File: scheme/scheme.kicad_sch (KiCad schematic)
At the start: 3 parts, among them U1 ESP32-WROOM-32, U2 PCM1808

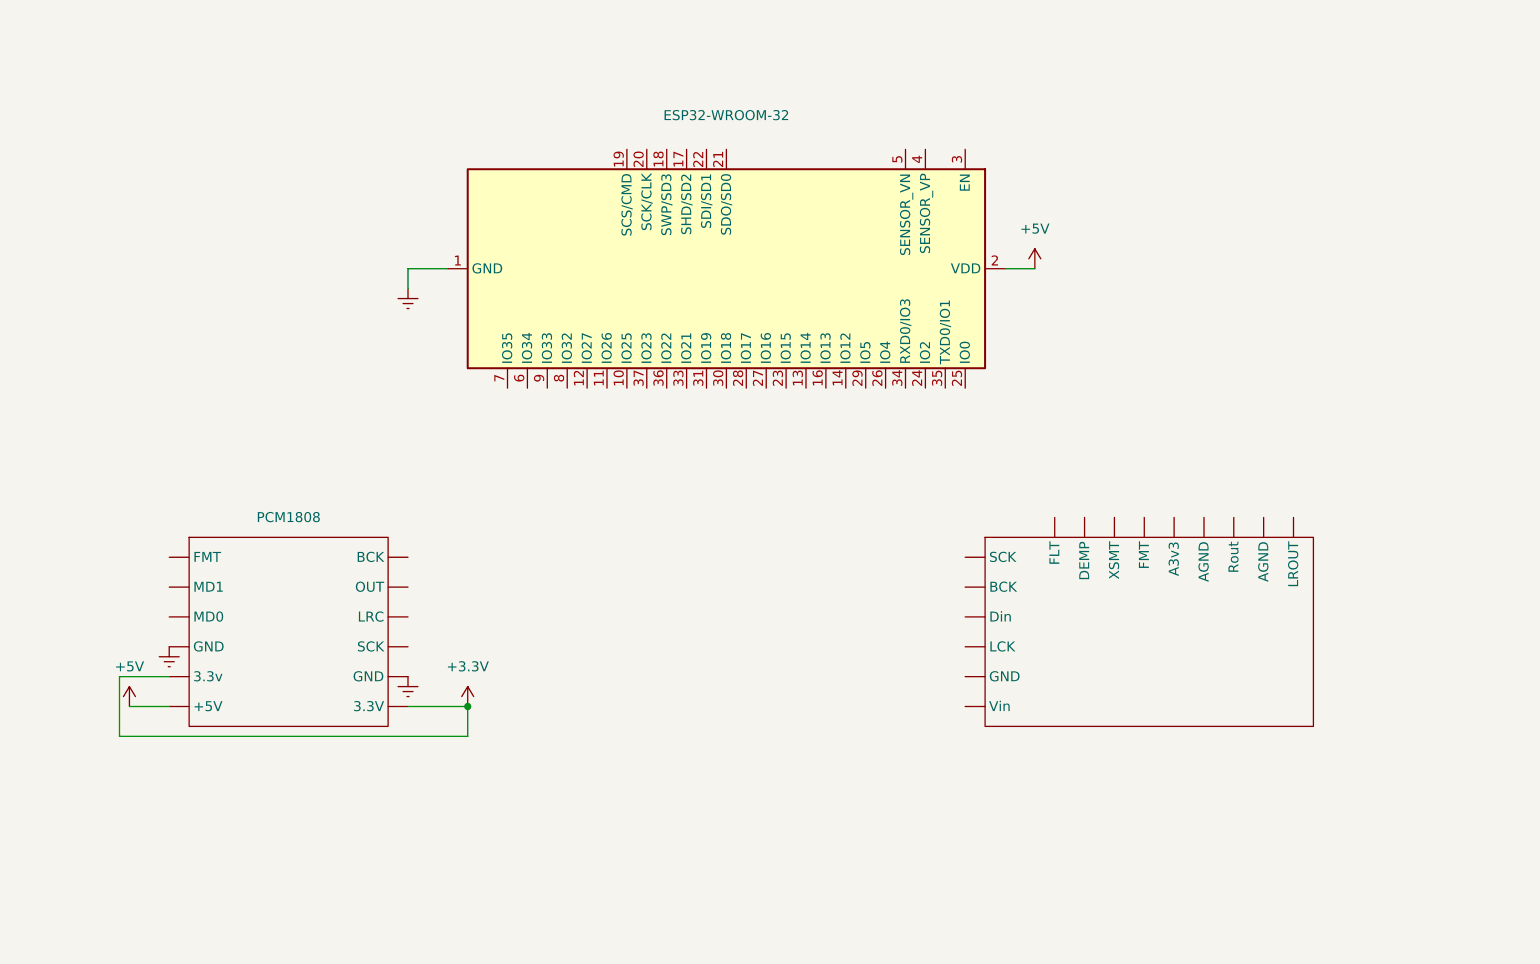
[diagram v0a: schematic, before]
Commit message: Add project scheme and update README
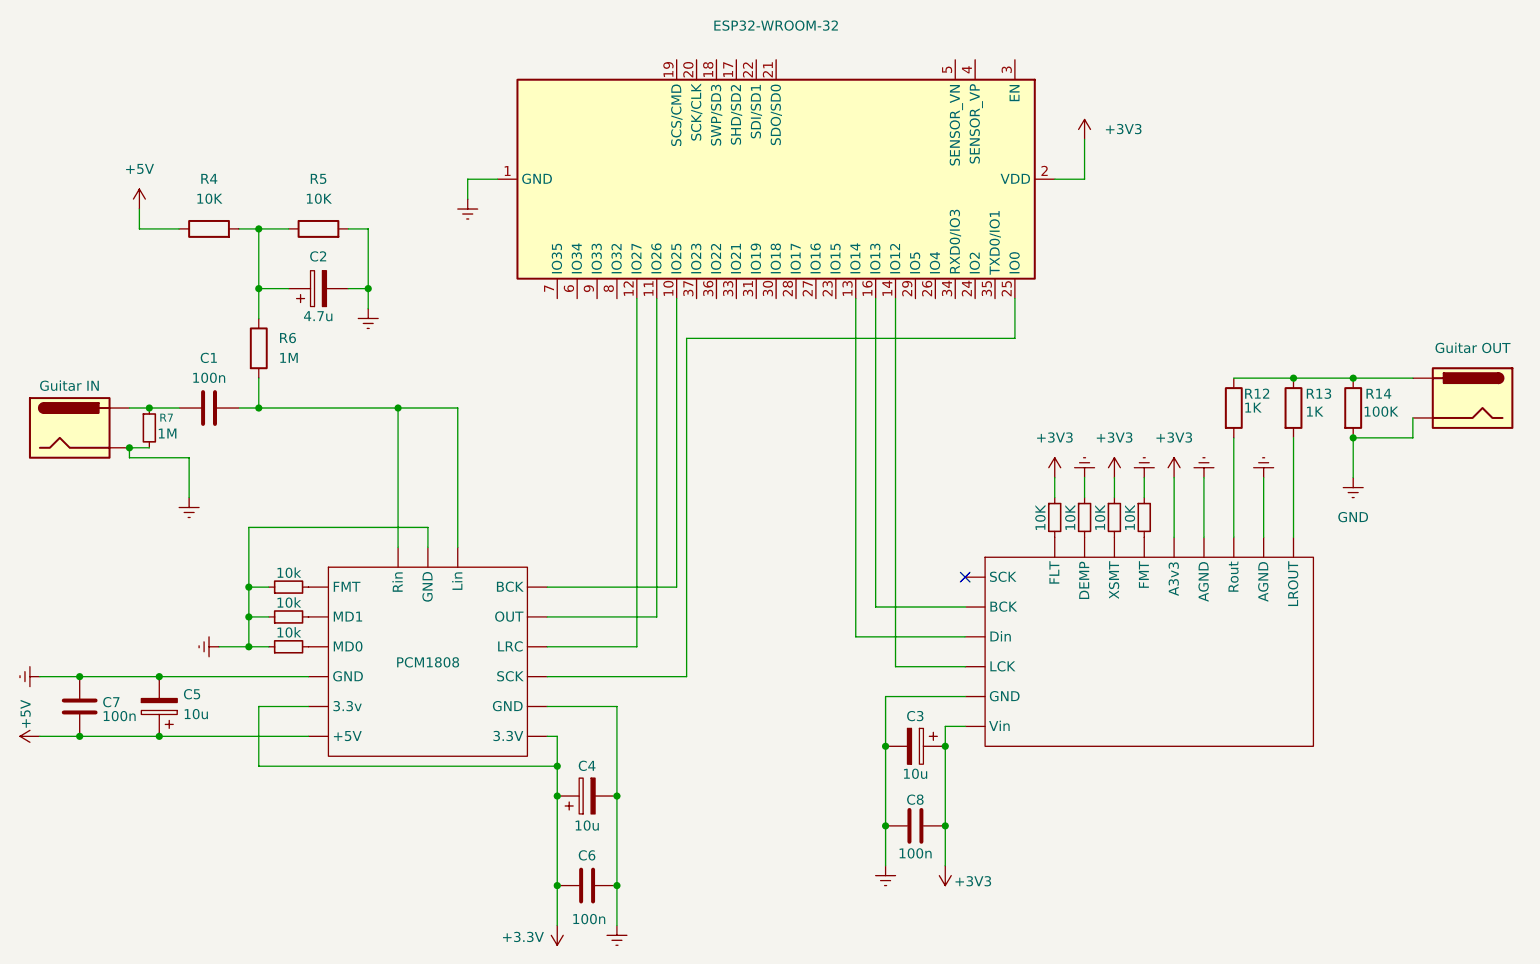
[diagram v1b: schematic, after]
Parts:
- added C1, C6, C7, C8: 100n, symbol Device:C
- added C2: 4.7u, symbol Device:C_Polarized
- added C3, C4, C5: 10u, symbol Device:C_Polarized
- added J1: Guitar IN, symbol Connector:Jack-DC
- added J2: Guitar OUT, symbol Connector:Jack-DC
- added R1, R2, R3: 10k, symbol Device:R_Small
- added R10, R11, R8, R9: 10K, symbol Device:R_Small
- added R12, R13: 1K, symbol Device:R
- added R14: 100K, symbol Device:R
- added R4, R5: 10K, symbol Device:R
- added R6: 1M, symbol Device:R
- added R7: 1M, symbol Device:R_Small
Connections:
- net +3.3V: now also C4.1, C6.1
- net +5V: now also C5.1, C7.1, R4.1; no longer U1.2 (VDD)
- net at U1.10 (IO25): now also U2. (3.3V)
- net at U1.11 (IO26): now also U2. (3.3V)
- net at U1.12 (IO27): now also U2. (3.3V)
- net at U1.13 (IO14): now also 1. (LROUT)
- net at U1.14 (IO12): now also 1. (LROUT)
- net at U1.16 (IO13): now also 1. (LROUT)
- net at U1.25 (IO0): now also U2. (3.3V)
- net GNDREF: now reaches 1. (LROUT)
- net GNDREF: now also C2.2, C3.2, C8.1, R11.1, R5.2, R9.1
- net GND: now reaches U2. (3.3V)
- net GND: now also J1.2, J2.2, R1.1, R14.2, R2.1, R3.1, R7.2
- new net: C2.1, R4.2, R5.1, R6.1
- new net: 1. (LROUT), R9.2
- new net: J2.1, R12.1, R13.1, R14.1
- new net: C1.1, J1.1, R7.1
- new net: 1. (LROUT), R10.2
- new net: C5.2, C7.2, U2. (3.3V)
- new net: C4.2, C6.2, U2. (3.3V)
- new net: 1. (LROUT), R8.2
- new net: 1. (LROUT), R11.2
- new net: 1. (LROUT), R13.2
- new net: 1. (LROUT), R12.2
- new net: R1.2, U2. (3.3V)
- new net: C1.2, R6.2, U2. (3.3V)
- new net: R3.2, U2. (3.3V)
- new net: R2.2, U2. (3.3V)
- new net +3V3: 1. (LROUT), C3.1, C8.2, R10.1, R8.1, U1.2 (VDD)
- no-connect marks 0 -> 1

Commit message: Implement distortion and overdrive audio effects
- Reduced buffer sizes for delay and reverb effects from 32768 to 16384 in delay.h.
- Removed setup.h and migrated its functionality to protocol_setup.h.
- Modified schematic to reflect changes in component values and connections.
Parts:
- U1: value ESP32-WROOM-32 -> ESP32-WROVER
- renumbered 1 to PCM5102
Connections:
- net at U1.10 (IO25): no longer U2. (3.3V)
- net at U1.11 (IO26): no longer U2. (3.3V)
- net at U1.12 (IO27): no longer U2. (3.3V)
- net at U1.13 (IO14): no longer PCM5102. (LROUT)
- net at U1.14 (IO12): no longer PCM5102. (LROUT)
- net at U1.16 (IO13): no longer PCM5102. (LROUT)
- net at U1.27 (IO16): now also U2. (3.3V)
- net at U1.28 (IO17): now also U2. (3.3V)
- net at U1.30 (IO18): now also U2. (3.3V)
- net at U1.33 (IO21): now also PCM5102. (LROUT)
- net at U1.36 (IO22): now also PCM5102. (LROUT)
- net at U1.37 (IO23): now also PCM5102. (LROUT)
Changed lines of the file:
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@@
-	(wire
-		(pts
-			(xy 172.72 119.38) (xy 163.83 119.38)
-		)
-		(stroke
-			(width 0)
-			(type default)
-		)
-	)
 	(wire
 		(pts
@@
 	(wire
 		(pts
+			(xy 151.13 72.39) (xy 151.13 83.82)
+		)
+		(stroke
+			(width 0)
+			(type default)
+		)
+	)
+	(wire
+		(pts
 			(xy 187.96 52.07) (xy 187.96 57.15)
 		)
@@
 	(wire
 		(pts
+			(xy 128.27 116.84) (xy 128.27 86.36)
+		)
+		(stroke
+			(width 0)
+			(type default)
+		)
+	)
+	(wire
+		(pts
 			(xy 170.18 129.54) (xy 170.18 127)
 		)
@@
 	(wire
 		(pts
-			(xy 119.38 109.22) (xy 135.89 109.22)
-		)
-		(stroke
-			(width 0)
-			(type default)
-		)
-	)
-	(wire
-		(pts
 			(xy 210.82 95.25) (xy 210.82 102.87)
 		)
@@
 	(wire
 		(pts
-			(xy 119.38 113.03) (xy 133.35 113.03)
+			(xy 148.59 72.39) (xy 148.59 86.36)
 		)
 		(stroke
@@
 	(wire
 		(pts
-			(xy 172.72 115.57) (xy 158.75 115.57)
-		)
-		(stroke
-			(width 0)
-			(type default)
-		)
-	)
-	(wire
-		(pts
 			(xy 96.52 63.5) (xy 93.98 63.5)
 		)
@@
 	(wire
 		(pts
-			(xy 137.16 77.47) (xy 179.07 77.47)
-		)
-		(stroke
-			(width 0)
-			(type default)
-		)
-	)
-	(wire
-		(pts
 			(xy 120.65 132.08) (xy 120.65 128.27)
 		)
@@
 	(wire
 		(pts
+			(xy 125.73 83.82) (xy 151.13 83.82)
+		)
+		(stroke
+			(width 0)
+			(type default)
+		)
+	)
+	(wire
+		(pts
+			(xy 125.73 113.03) (xy 125.73 83.82)
+		)
+		(stroke
+			(width 0)
+			(type default)
+		)
+	)
+	(wire
+		(pts
+			(xy 128.27 86.36) (xy 148.59 86.36)
+		)
+		(stroke
+			(width 0)
+			(type default)
+		)
+	)
+	(wire
+		(pts
 			(xy 187.96 95.25) (xy 187.96 97.79)
 		)
@@
 	(wire
 		(pts
+			(xy 119.38 113.03) (xy 125.73 113.03)
+		)
+		(stroke
+			(width 0)
+			(type default)
+		)
+	)
+	(wire
+		(pts
 			(xy 81.28 113.03) (xy 81.28 116.84)
 		)
@@
 	(wire
 		(pts
+			(xy 172.72 111.76) (xy 143.51 111.76)
+		)
+		(stroke
+			(width 0)
+			(type default)
+		)
+	)
+	(wire
+		(pts
 			(xy 207.01 90.17) (xy 207.01 102.87)
 		)
@@
 	(wire
 		(pts
-			(xy 133.35 113.03) (xy 133.35 72.39)
-		)
-		(stroke
-			(width 0)
-			(type default)
-		)
-	)
-	(wire
-		(pts
-			(xy 137.16 120.65) (xy 137.16 77.47)
+			(xy 123.19 81.28) (xy 153.67 81.28)
 		)
 		(stroke
@@
 	(wire
 		(pts
+			(xy 130.81 88.9) (xy 179.07 88.9)
+		)
+		(stroke
+			(width 0)
+			(type default)
+		)
+	)
+	(wire
+		(pts
 			(xy 69.85 120.65) (xy 88.9 120.65)
 		)
@@
 	(wire
 		(pts
+			(xy 179.07 88.9) (xy 179.07 72.39)
+		)
+		(stroke
+			(width 0)
+			(type default)
+		)
+	)
+	(wire
+		(pts
 			(xy 162.56 123.19) (xy 172.72 123.19)
 		)
@@
 	(wire
 		(pts
+			(xy 119.38 109.22) (xy 123.19 109.22)
+		)
+		(stroke
+			(width 0)
+			(type default)
+		)
+	)
+	(wire
+		(pts
 			(xy 120.65 135.89) (xy 120.65 147.32)
 		)
@@
 	(wire
 		(pts
-			(xy 158.75 115.57) (xy 158.75 72.39)
-		)
-		(stroke
-			(width 0)
-			(type default)
-		)
-	)
-	(wire
-		(pts
 			(xy 88.9 124.46) (xy 82.55 124.46)
 		)
@@
 	(wire
 		(pts
-			(xy 179.07 77.47) (xy 179.07 72.39)
+			(xy 172.72 115.57) (xy 138.43 115.57)
+		)
+		(stroke
+			(width 0)
+			(type default)
+		)
+	)
+	(wire
+		(pts
+			(xy 140.97 72.39) (xy 140.97 119.38)
 		)
 		(stroke
@@
 	(wire
 		(pts
+			(xy 119.38 120.65) (xy 130.81 120.65)
+		)
+		(stroke
+			(width 0)
+			(type default)
+		)
+	)
+	(wire
+		(pts
 			(xy 222.25 90.17) (xy 222.25 95.25)
 		)
@@
 	(wire
 		(pts
-			(xy 161.29 72.39) (xy 161.29 111.76)
-		)
-		(stroke
-			(width 0)
-			(type default)
-		)
-	)
-	(wire
-		(pts
-			(xy 130.81 116.84) (xy 130.81 72.39)
+			(xy 153.67 72.39) (xy 153.67 81.28)
+		)
+		(stroke
+			(width 0)
+			(type default)
+		)
+	)
+	(wire
+		(pts
+			(xy 130.81 120.65) (xy 130.81 88.9)
 		)
 		(stroke
@@
 	(wire
 		(pts
-			(xy 119.38 120.65) (xy 137.16 120.65)
-		)
-		(stroke
-			(width 0)
-			(type default)
-		)
-	)
-	(wire
-		(pts
-			(xy 119.38 116.84) (xy 130.81 116.84)
-		)
-		(stroke
-			(width 0)
-			(type default)
-		)
-	)
-	(wire
-		(pts
 			(xy 214.63 90.17) (xy 214.63 102.87)
 		)
@@
 	(wire
 		(pts
+			(xy 119.38 116.84) (xy 128.27 116.84)
+		)
+		(stroke
+			(width 0)
+			(type default)
+		)
+	)
+	(wire
+		(pts
 			(xy 184.15 57.15) (xy 187.96 57.15)
 		)
@@
 	(wire
 		(pts
+			(xy 172.72 119.38) (xy 140.97 119.38)
+		)
+		(stroke
+			(width 0)
+			(type default)
+		)
+	)
+	(wire
+		(pts
 			(xy 162.56 139.7) (xy 162.56 144.78)
 		)
@@
 	(wire
 		(pts
-			(xy 163.83 119.38) (xy 163.83 72.39)
-		)
-		(stroke
-			(width 0)
-			(type default)
-		)
-	)
-	(wire
-		(pts
 			(xy 104.14 104.14) (xy 104.14 101.6)
 		)
@@
 	(wire
 		(pts
-			(xy 135.89 109.22) (xy 135.89 72.39)
-		)
-		(stroke
-			(width 0)
-			(type default)
-		)
-	)
-	(wire
-		(pts
 			(xy 82.55 132.08) (xy 120.65 132.08)
 		)
@@
 	(wire
 		(pts
+			(xy 143.51 111.76) (xy 143.51 72.39)
+		)
+		(stroke
+			(width 0)
+			(type default)
+		)
+	)
+	(wire
+		(pts
 			(xy 66.04 92.71) (xy 73.66 92.71)
 		)
@@
 	(wire
 		(pts
-			(xy 172.72 111.76) (xy 161.29 111.76)
-		)
-		(stroke
-			(width 0)
-			(type default)
-		)
-	)
-	(wire
-		(pts
 			(xy 107.95 86.36) (xy 107.95 104.14)
 		)
@@
 	(wire
 		(pts
+			(xy 138.43 115.57) (xy 138.43 72.39)
+		)
+		(stroke
+			(width 0)
+			(type default)
+		)
+	)
+	(wire
+		(pts
 			(xy 162.56 129.54) (xy 162.56 139.7)
 		)
@@
 		(pts
 			(xy 120.65 152.4) (xy 120.65 147.32)
+		)
+		(stroke
+			(width 0)
+			(type default)
+		)
+	)
+	(wire
+		(pts
+			(xy 123.19 109.22) (xy 123.19 81.28)
 		)
 		(stroke
@@
 			)
 		)
-		(property "Value" "ESP32-WROOM-32"
+		(property "Value" "ESP32-WROVER"
 			(at 148.59 37.592 90)
 			(effects
@@
 		(on_board yes)
 		(dnp no)
-		(fields_autoplaced yes)
-		(property "Reference" "1"
-			(at 177.038 88.646 0)
-			(effects
-				(font
-					(size 1.27 1.27)
+		(property "Reference" "PCM5102"
+			(at 187.452 118.11 0)
+			(effects
+				(font
+					(size 1.27 1.27)
+					(color 255 0 244 1)
 				)
 				(justify left)
-				(hide yes)
 			)
 		)
@@
 			(project ""
 				(path "/8f73dd53-d14a-43de-b574-d1d2cf4856c7"
-					(reference "1")
+					(reference "PCM5102")
 					(unit 1)
 				)
